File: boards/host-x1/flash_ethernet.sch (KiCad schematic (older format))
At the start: 37 parts, among them J4 BEL_FUSE_0826-1G1T-23-F, U2 XC7A100T-1FTG256C, U8 KSZ9031RN

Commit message: Finished initial work on schematic. Ready for pre-layout design review
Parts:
- added C104, C105, C110: 0.47 uF, symbol C
- added C106, C107, C108, C109: 0.1 uF, symbol C
- added D2, D3, D4, D5: LED, symbol LED
- added Q1, Q2, Q3, Q4: SSM6N58NU, symbol SSM6N58NU_DUAL_NMOS
- added R37, R38, R39, R40, R46, R50: 270, symbol R
- added R41, R42, R44, R51, R52, R53, R54: 33, symbol R
- added R43: 1K, symbol R
- added R45: 12.1K, symbol R
- added R47, R49: 1k, symbol R
- added R48: 10k, symbol R
- added U10: DSC6102CI2A-100.0000, symbol OSC
- added U11: S25FS064S_BGA, symbol S25FS064S_BGA
- added U9: DSC6101CI2A-025.0000, symbol OSC
- R28: value 1K -> 4.7k
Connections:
- net 1V8: now also C104.1, C105.1, C110.1, R43.2, R48.1, R49.1, U10.1 (E/D#), U10.4 (Vdd), U11.B4 (VDD), U9.1 (E/D#), U9.4 (Vdd)
- net 3V3: now also J4.14 (LED1_P), J4.16 (LED2_P), R37.2, R38.2, R39.2, R40.2
- net A1V2: no longer C91.1, C96.1, L7.1
- net A1V2_PLL: now also C91.1, C96.1, L7.1
- net ETH_A_N: now also J4.10 (CH1_N)
- net ETH_A_P: now also J4.11 (CH1_P)
- net ETH_B_N: now also J4.5 (CH2_N)
- net ETH_B_P: now also J4.4 (CH2_P)
- net ETH_C_N: now also J4.2 (CH3_N)
- net ETH_C_P: now also J4.3 (CH3_P)
- net ETH_D_N: now also J4.9 (CH4_N)
- net ETH_D_P: now also J4.8 (CH4_P)
- net FLASH_CS_N: now also U11.C2 (CS_N)
- net FLASH_DQ0: now also R51.1
- net FLASH_DQ1: now also R52.1
- net FLASH_DQ2: now also R53.1
- net FLASH_DQ3: now also R54.1
- net FLASH_SCK: now also U11.B2 (SCK)
- net GND: now also J4.17 (SHLD), C104.2, C105.2, C106.2, C107.2, C108.2, C109.2, C110.2, Q1.S2 (S), Q2.S1 (S), Q2.S2 (S), Q3.S1 (S), Q3.S2 (S), Q4.S1 (S), R45.1, R47.1, U10.2 (Vss), U11.B3 (VSS), U9.2 (Vss)
- net ETH_ACTIVITY_LED: now reaches U2.M6 (IO_L19P_T3_A10_D26_14)
- net ETH_ACTIVITY_LED: now also Q3.G2 (G)
- net CLK_100MHZ: now reaches U2.N11 (IO_L13P_T2_MRCC_14)
- net CLK_100MHZ: now also R42.1
- net ETH_LINK_LED: now reaches U2.N6 (IO_L19N_T3_A09_D25_VREF_14)
- net ETH_LINK_LED: now also Q4.G1 (G)
- net ETH_INT_N: now reaches U2.N9 (IO_L18P_T2_A12_D28_14)
- net ETH_INT_N: now also R44.1
- net RGMII_TXD3: now reaches U2.P10 (IO_L14P_T2_SRCC_14)
- net RGMII_TXD3: now also U8.22 (TXD3)
- net RGMII_TXD2: now reaches U2.P11 (IO_L14N_T2_SRCC_14)
- net RGMII_TXD2: now also U8.21 (TXD2)
- net LED0: now reaches U2.P6 (IO_25_14)
- net LED0: now also Q1.G2 (G)
- net ETH_RST_N: now reaches U2.P9 (IO_L18N_T2_A11_D27_14)
- net ETH_RST_N: now also U8.42 (RESET_N)
- net ETH_MDIO: now reaches U2.R10 (IO_L17P_T2_A14_D30_14)
- net ETH_MDIO: now also U8.37 (MDIO), R43.1
- net ETH_MDC: now reaches U2.R11 (IO_L17N_T2_A13_D29_14)
- net ETH_MDC: now also U8.36 (MDC)
- net RGMII_TXD1: now reaches U2.R12 (IO_L15P_T2_DQS_RDWR_B_14)
- net RGMII_TXD1: now also U8.20 (TXD1)
- net RGMII_TX_EN: now reaches U2.R13 (IO_L16P_T2_CSI_B_14)
- net RGMII_TX_EN: now also U8.25 (TX_EN)
- net LED2: now reaches U2.R6 (IO_L24P_T3_A01_D17_14)
- net LED2: now also Q2.G2 (G)
- net LED1: now reaches U2.R7 (IO_L24N_T3_A00_D16_14)
- net LED1: now also Q2.G1 (G)
- net RGMII_TXD0: now reaches U2.T12 (IO_L15N_T2_DQS_DOUT_CSO_B_14)
- net RGMII_TXD0: now also U8.19 (TXD0)
- net RGMII_TX_CLK: now reaches U2.T13 (IO_L16N_T2_A15_D31_14)
- net RGMII_TX_CLK: now also U8.24 (GTX_CLK)
- net LED3: now reaches U2.T5 (IO_L23N_T3_A02_D18_14)
- net LED3: now also Q3.G1 (G)
- net at U8.15 (LED2/PHYAD1): now also R47.2
- net at U8.17 (LED1/PHYAD0): now also R48.2
- net at U8.38 (INT_N): now also R44.2
- net at U8.41 (CLK125_NDO/LED_MODE): now also R49.2
- net CLK_25MHZ: now reaches U8.46 (XI)
- net CLK_25MHZ: now also R41.1
- net at U8.48 (ISET): now also R45.2
- net ETH_C_TAP: now reaches J4.1 (CH3_TAP)
- net ETH_C_TAP: now also C108.1
- net ETH_A_TAP: now reaches J4.12 (CH1_TAP)
- net ETH_A_TAP: now also C106.1
- net ETH_LED_1_N: now reaches J4.13 (LED1_N)
- net ETH_LED_1_N: now also R46.2
- net ETH_LED_2_N: now reaches J4.15 (LED2_N)
- net ETH_LED_2_N: now also R50.2
- net ETH_B_TAP: now reaches J4.6 (CH2_TAP)
- net ETH_B_TAP: now also C107.1
- net ETH_D_TAP: now reaches J4.7 (CH4_TAP)
- net ETH_D_TAP: now also C109.1
- new net: D2.1 (K), Q1.D2 (D)
- new net: D2.2 (A), R37.1
- new net: D3.1 (K), Q2.D1 (D)
- new net: D3.2 (A), R38.1
- new net: D4.1 (K), Q2.D2 (D)
- new net: D4.2 (A), R39.1
- new net: D5.1 (K), Q3.D1 (D)
- new net: D5.2 (A), R40.1
- new net: R41.2, U9.3 (CLK)
- new net: R42.2, U10.3 (CLK)
- new net: Q3.D2 (D), R46.1
- new net: Q4.D1 (D), R50.1
- new net: R53.2, U11.C4 (WP_N/DQ2)
- new net: R52.2, U11.D2 (MISO/DQ1)
- new net: R51.2, U11.D3 (MOSI/DQ0)
- new net: R54.2, U11.D4 (RESET_N/DQ3)
- no-connect marks 1 -> 24
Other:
- note added: "Debug indicator LEDs"
- note added: "Oscillator decoupling"
- moved on the sheet: C100, C101, C102, C103, C82, C83, C84, C85, C86, C87, C88, C89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

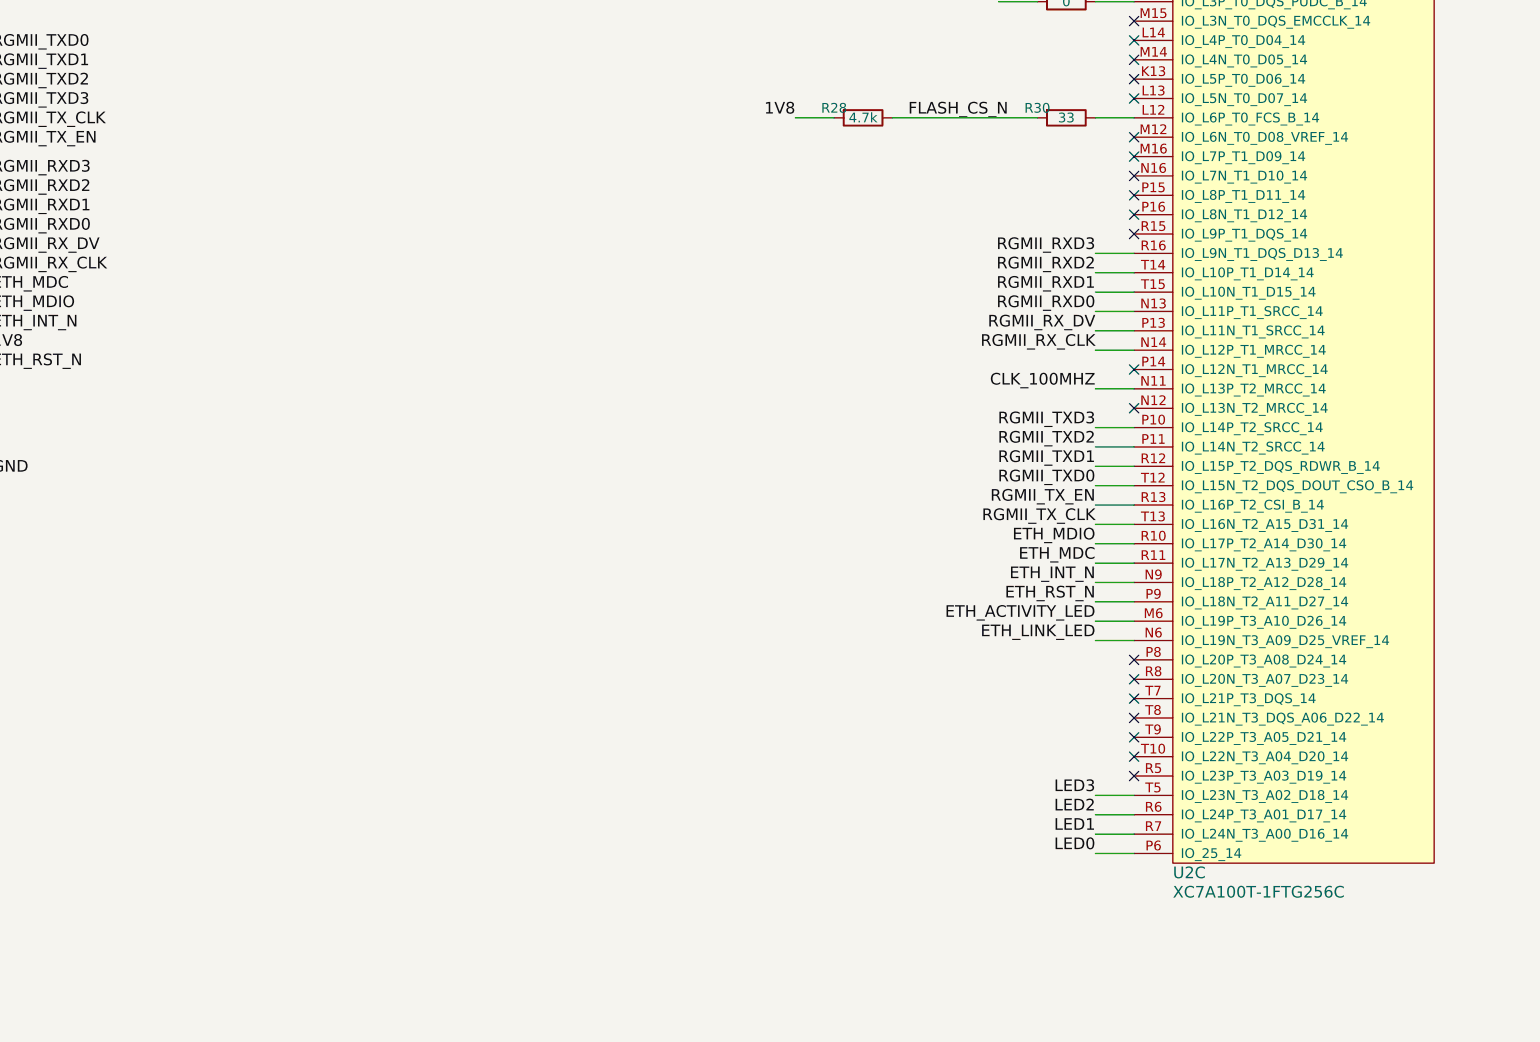
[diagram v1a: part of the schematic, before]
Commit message: Added more test points, various tweaks for debuggability. Clarified values for design review
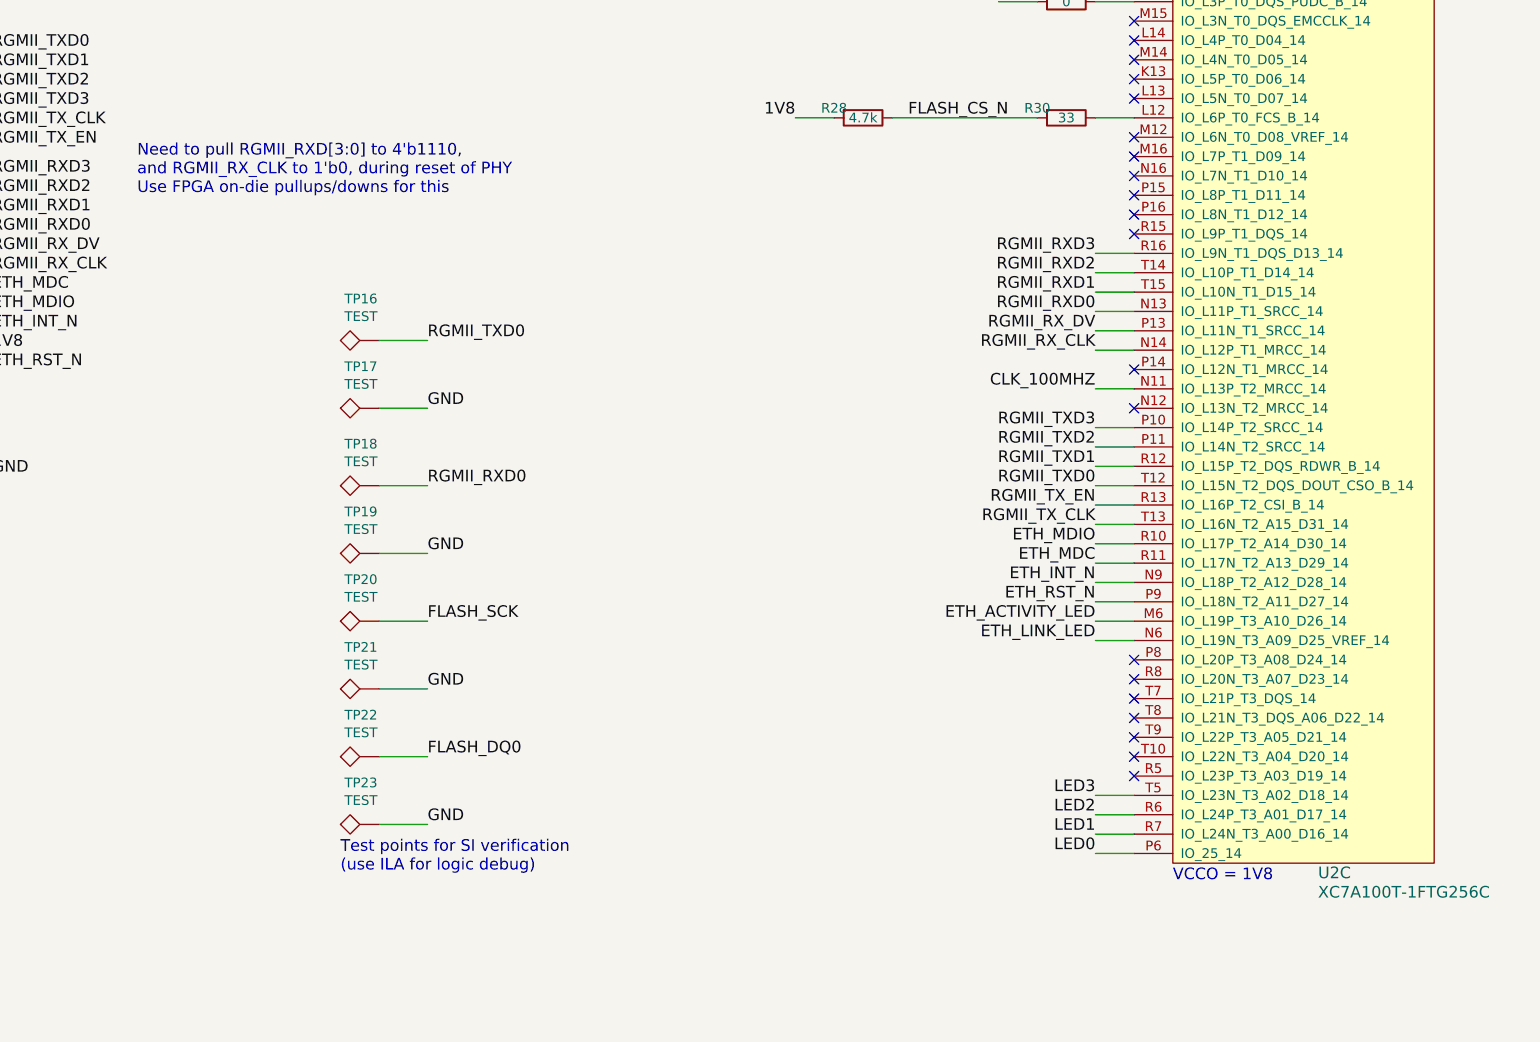
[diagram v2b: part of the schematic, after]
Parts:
- added TP16, TP17, TP18, TP19, TP20, TP21, TP22, TP23: TEST, symbol TEST
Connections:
- net FLASH_DQ0: now also TP22.1
- net FLASH_SCK: now also TP20.1
- net GND: now also TP17.1, TP19.1, TP21.1, TP23.1
- net RGMII_RXD0: now also TP18.1
- net RGMII_TXD0: now also TP16.1
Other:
- note added: "Need to pull RGMII_RXD[3:0] to 4'b1110,\nand RGMII_RX_CLK to 1'b0, during reset of PHY\nUse FPGA on-die pullups/downs for this"
- note added: "Test points for SI verification\n(use ILA for logic debug)"
- note added: "VCCO = 1V8"
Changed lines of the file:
@@
 Sheet 6 6
 Title "STARSHIPRAIDER Single-Lane Host"
-Date "2017-05-06"
+Date "2017-05-07"
 Rev "0.1"
 Comp "Andrew D. Zonenberg"
@@
 AR Path="/590BFAE6/590E87C3" Ref="U?"  Part="3"
 AR Path="/590E8635/590E87C3" Ref="U2"  Part="3"
-F 0 "U2" H 14200 5650 60  0000 L CNN
-F 1 "XC7A100T-1FTG256C" H 14200 5550 60  0000 L CNN
+F 0 "U2" H 14950 5650 60  0000 L CNN
+F 1 "XC7A100T-1FTG256C" H 14950 5550 60  0000 L CNN
 F 2 "" H 14200 5750 60  0000 C CNN
 F 3 "" H 14200 5750 60  0000 C CNN
@@
 Wire Wire Line
 	8150 7300 7950 7300
+Text Notes 14200 5900 0    60   ~ 0
+VCCO = 1V8
+$Comp
+L TEST TP16
+U 1 1 5913F2EA
+P 10100 3100
+F 0 "TP16" V 10315 3194 50  0000 C CNN
+F 1 "TEST" V 10224 3194 50  0000 C CNN
+F 2 "" H 10100 3100 50  0000 C CNN
+F 3 "" H 10100 3100 50  0000 C CNN
+	1    10100 3100
+	0    -1   -1   0
+$EndComp
+Text Label 10350 3100 0    60   ~ 0
+RGMII_TXD0
+Wire Wire Line
+	10350 3100 10100 3100
+$Comp
+L TEST TP17
+U 1 1 5913FA7F
+P 10100 3450
+F 0 "TP17" V 10315 3544 50  0000 C CNN
+F 1 "TEST" V 10224 3544 50  0000 C CNN
+F 2 "" H 10100 3450 50  0000 C CNN
+F 3 "" H 10100 3450 50  0000 C CNN
+	1    10100 3450
+	0    -1   -1   0
+$EndComp
+Text Label 10350 3450 0    60   ~ 0
+GND
+Wire Wire Line
+	10350 3450 10100 3450
+$Comp
+L TEST TP18
+U 1 1 5913FD07
+P 10100 3850
+F 0 "TP18" V 10315 3944 50  0000 C CNN
+F 1 "TEST" V 10224 3944 50  0000 C CNN
+F 2 "" H 10100 3850 50  0000 C CNN
+F 3 "" H 10100 3850 50  0000 C CNN
+	1    10100 3850
+	0    -1   -1   0
+$EndComp
+Text Label 10350 3850 0    60   ~ 0
+RGMII_RXD0
+Wire Wire Line
+	10350 3850 10100 3850
+$Comp
+L TEST TP19
+U 1 1 5913FD0F
+P 10100 4200
+F 0 "TP19" V 10315 4294 50  0000 C CNN
+F 1 "TEST" V 10224 4294 50  0000 C CNN
+F 2 "" H 10100 4200 50  0000 C CNN
+F 3 "" H 10100 4200 50  0000 C CNN
+	1    10100 4200
+	0    -1   -1   0
+$EndComp
+Text Label 10350 4200 0    60   ~ 0
+GND
+Wire Wire Line
+	10350 4200 10100 4200
+$Comp
+L TEST TP20
+U 1 1 591401A2
+P 10100 4550
+F 0 "TP20" V 10315 4644 50  0000 C CNN
+F 1 "TEST" V 10224 4644 50  0000 C CNN
+F 2 "" H 10100 4550 50  0000 C CNN
+F 3 "" H 10100 4550 50  0000 C CNN
+	1    10100 4550
+	0    -1   -1   0
+$EndComp
+Text Label 10350 4550 0    60   ~ 0
+FLASH_SCK
+Wire Wire Line
+	10350 4550 10100 4550
+$Comp
+L TEST TP21
+U 1 1 591401AA
+P 10100 4900
+F 0 "TP21" V 10315 4994 50  0000 C CNN
+F 1 "TEST" V 10224 4994 50  0000 C CNN
+F 2 "" H 10100 4900 50  0000 C CNN
+F 3 "" H 10100 4900 50  0000 C CNN
+	1    10100 4900
+	0    -1   -1   0
+$EndComp
+Text Label 10350 4900 0    60   ~ 0
+GND
+Wire Wire Line
+	10350 4900 10100 4900
+$Comp
+L TEST TP22
+U 1 1 59140436
+P 10100 5250
+F 0 "TP22" V 10315 5344 50  0000 C CNN
+F 1 "TEST" V 10224 5344 50  0000 C CNN
+F 2 "" H 10100 5250 50  0000 C CNN
+F 3 "" H 10100 5250 50  0000 C CNN
+	1    10100 5250
+	0    -1   -1   0
+$EndComp
+Text Label 10350 5250 0    60   ~ 0
+FLASH_DQ0
+Wire Wire Line
+	10350 5250 10100 5250
+$Comp
+L TEST TP23
+U 1 1 5914043E
+P 10100 5600
+F 0 "TP23" V 10315 5694 50  0000 C CNN
+F 1 "TEST" V 10224 5694 50  0000 C CNN
+F 2 "" H 10100 5600 50  0000 C CNN
+F 3 "" H 10100 5600 50  0000 C CNN
+	1    10100 5600
+	0    -1   -1   0
+$EndComp
+Text Label 10350 5600 0    60   ~ 0
+GND
+Wire Wire Line
+	10350 5600 10100 5600
+Text Notes 8850 2350 0    60   ~ 0
+Need to pull RGMII_RXD[3:0] to 4'b1110,\nand RGMII_RX_CLK to 1'b0, during reset of PHY\nUse FPGA on-die pullups/downs for this
+Text Notes 9900 5850 0    60   ~ 0
+Test points for SI verification\n(use ILA for logic debug)
 $EndSCHEMATC
